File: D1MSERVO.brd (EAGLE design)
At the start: 48.3 x 33 mm, 57 parts, among them IC1 PCA9685

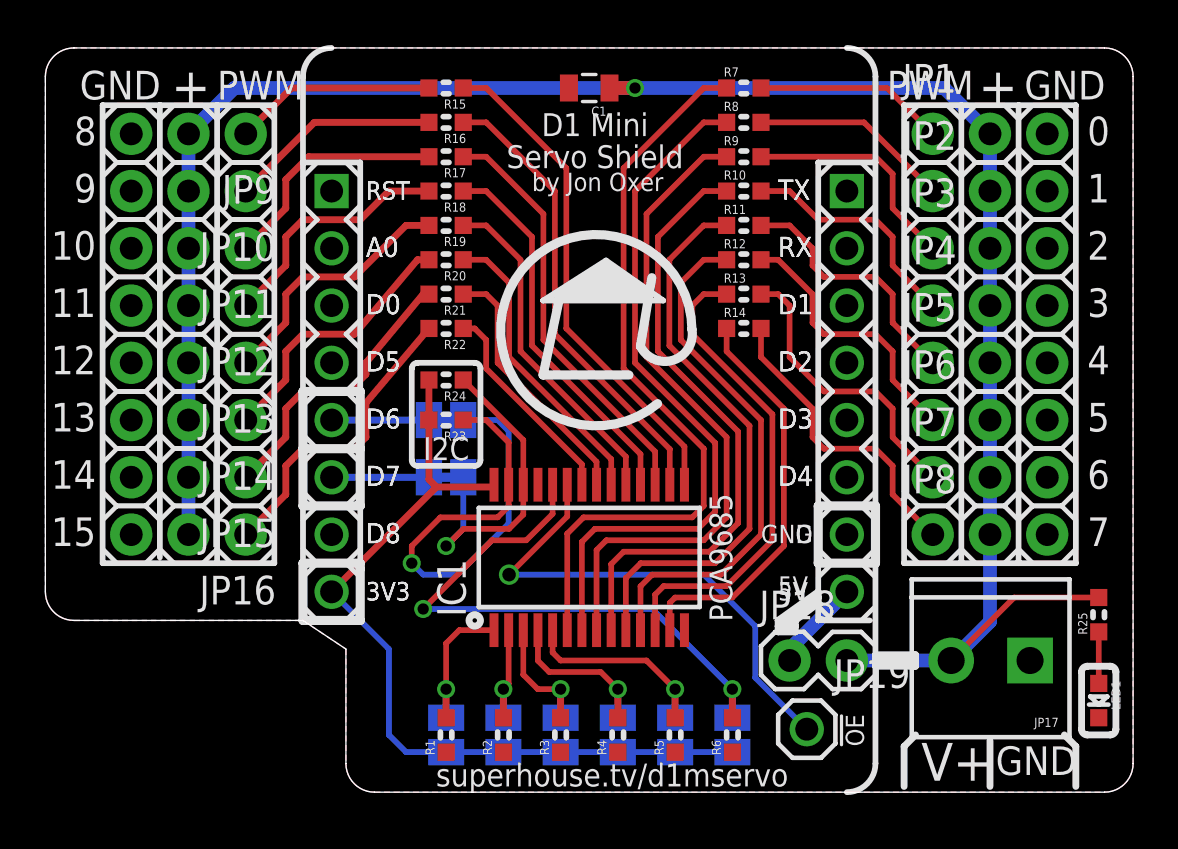
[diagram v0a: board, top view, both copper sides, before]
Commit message: Changed I2C pins
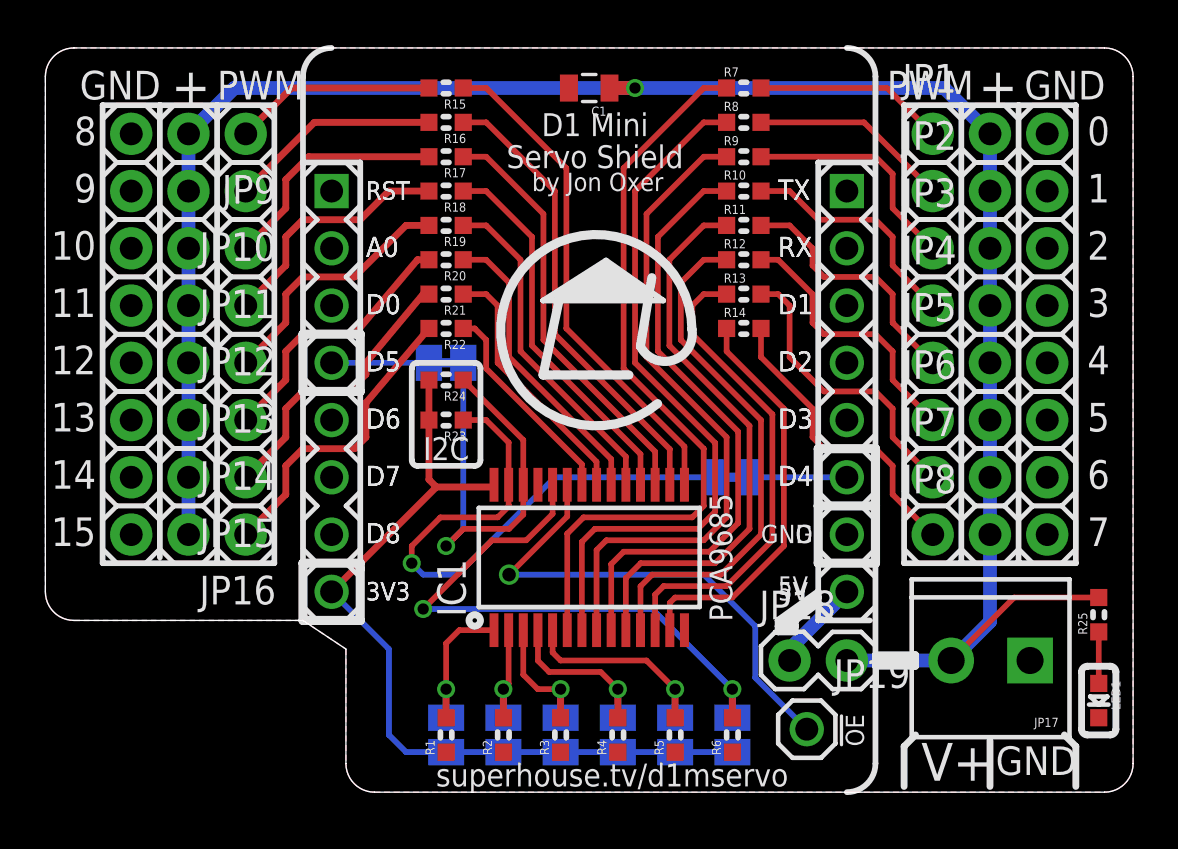
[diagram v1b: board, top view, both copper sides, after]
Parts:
- moved SJ7 13.0 mm to (30.5, 14.0), turned to 0 degrees
- moved SJ8 5.08 mm to (17.8, 19.1)
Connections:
- net D4: now also SJ7.1
- net D5: now also SJ8.1
- net D6: no longer SJ7.1
- net D7: no longer SJ8.1
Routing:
- net SCL: track 14.4 -> 19.5 mm
- net D7: track 4.32 -> 0.00 mm
- net D6: track 4.32 -> 0.00 mm
- net D5: track 0.00 -> 4.32 mm
- net D4: track 0.00 -> 4.32 mm
- net SDA: track 22.9 -> 26.5 mm
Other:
- board text added: "(C)2016 SuperHouse Automation Pty Ltd"
- board text added: "SCL: D5 SDA: D4"
- board text removed: "(C)2016 SuperHouse Pty Ltd"

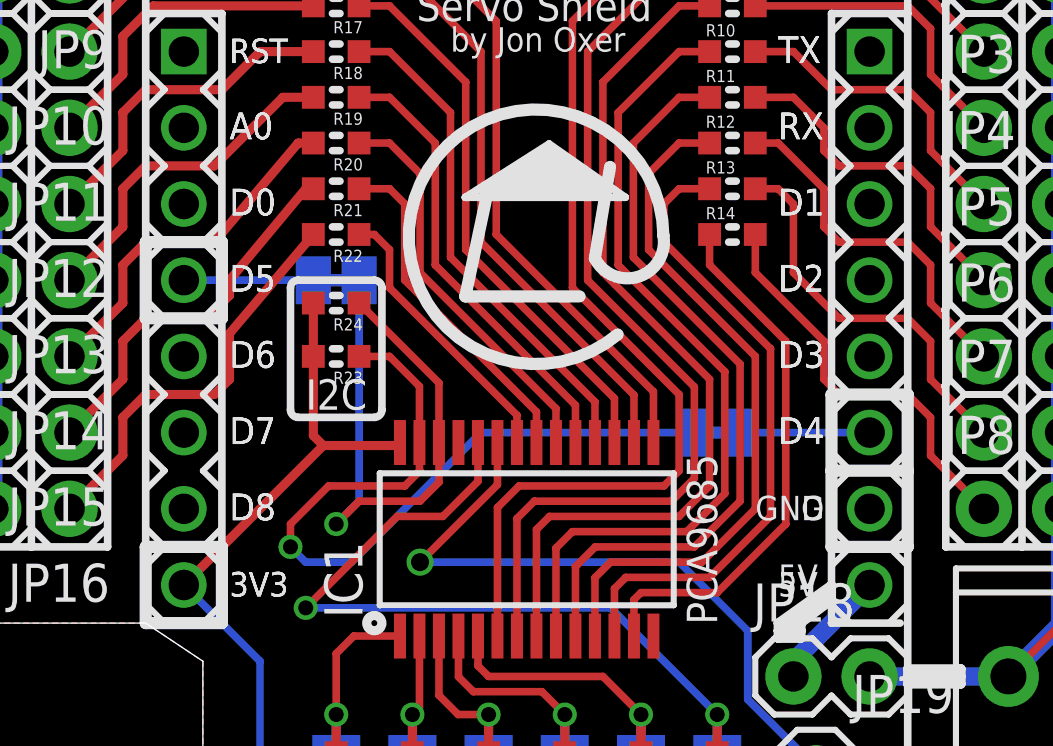
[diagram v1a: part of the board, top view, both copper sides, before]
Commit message: Changed I2C pins (again) to match ESP12E like on the D1 Mini and D1 R2
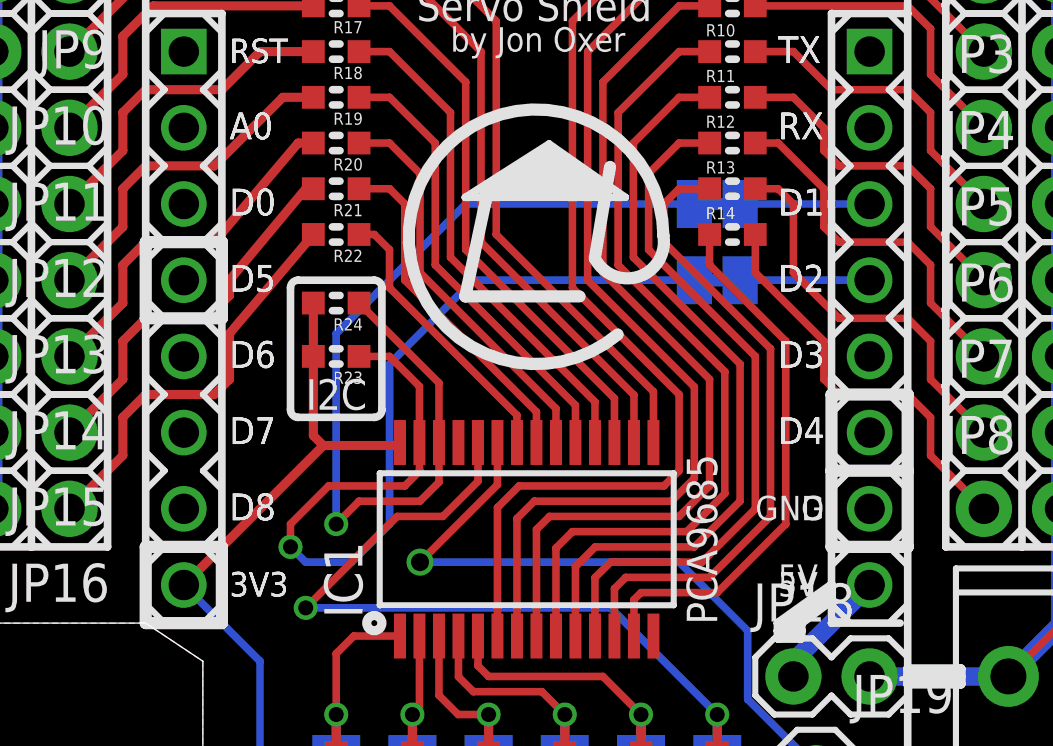
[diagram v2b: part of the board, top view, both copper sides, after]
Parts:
- moved SJ8 13.0 mm to (30.5, 21.6), turned to 0 degrees
- moved SJ7 5.08 mm to (30.5, 19.1)
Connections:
- net D1: now also SJ8.1
- net D2: now also SJ7.1
- net D4: no longer SJ7.1
- net D5: no longer SJ8.1
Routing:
- net SCL: track 19.5 -> 31.2 mm
- net SDA: track 26.5 -> 31.8 mm
- net D5: track 4.32 -> 0.00 mm
- net D4: track 4.32 -> 0.00 mm
- net D2: track 0.00 -> 4.32 mm
- net D1: track 0.00 -> 4.32 mm
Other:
- board text added: "SCL: D1 SDA: D2"
- board text removed: "SCL: D5 SDA: D4"
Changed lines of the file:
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@@
 <grid distance="0.01" unitdist="inch" unit="inch" style="lines" multiple="1" display="yes" altdistance="5" altunitdist="mil" altunit="mil"/>
 <layers>
-<layer number="1" name="Top" color="4" fill="1" visible="no" active="yes"/>
+<layer number="1" name="Top" color="4" fill="1" visible="yes" active="yes"/>
 <layer number="2" name="Route2" color="1" fill="3" visible="no" active="no"/>
 <layer number="3" name="Route3" color="4" fill="3" visible="no" active="no"/>
@@
 <text x="27.94" y="5.08" size="1.016" layer="22" font="vector" ratio="12" rot="MR0" align="bottom-center">A4</text>
 <text x="30.48" y="5.08" size="1.016" layer="22" font="vector" ratio="12" rot="MR0" align="bottom-center">A5</text>
-<text x="22.352" y="18.542" size="1.016" layer="22" font="vector" ratio="12" rot="MR0">SCL</text>
+<text x="28.448" y="21.082" size="1.016" layer="22" font="vector" ratio="12" rot="MR0">SCL</text>
 <text x="14.224" y="26.289" size="0.8128" layer="22" font="vector" ratio="15" rot="MR0" align="bottom-right">RST</text>
 <text x="14.224" y="18.669" size="0.889" layer="22" font="vector" ratio="15" rot="MR0" align="bottom-right">D5</text>
@@
 <wire x1="6.35" y1="9.652" x2="6.35" y2="8.636" width="0.254" layer="22"/>
 <wire x1="6.858" y1="9.144" x2="5.842" y2="9.144" width="0.254" layer="22"/>
-<text x="27.686" y="31.496" size="1.016" layer="22" font="vector" ratio="12" distance="36" rot="MR270">(C)2016 SuperHouse
+<text x="24.892" y="26.416" size="1.016" layer="22" font="vector" ratio="12" distance="36" rot="MR270">(C)2016 SuperHouse
 Automation Pty Ltd</text>
 <text x="24.384" y="27.686" size="1.016" layer="21" font="vector" ratio="18" distance="40" align="bottom-center">D1 Mini
@@
 <text x="21.336" y="31.496" size="0.8128" layer="22" font="vector" ratio="18" rot="MR0">v1.0</text>
 <text x="21.336" y="30.226" size="0.8128" layer="22" font="vector" ratio="18" rot="MR0">SKU: D1MSERVO</text>
-<text x="28.448" y="13.462" size="1.016" layer="22" font="vector" ratio="12" rot="MR0">SDA</text>
+<text x="28.448" y="18.542" size="1.016" layer="22" font="vector" ratio="12" rot="MR0">SDA</text>
 <wire x1="11.43" y1="17.78" x2="11.43" y2="7.62" width="0.254" layer="22"/>
 <wire x1="11.43" y1="17.78" x2="11.43" y2="20.32" width="0.4064" layer="22"/>
@@
 <wire x1="34.29" y1="15.24" x2="36.83" y2="15.24" width="0.4064" layer="22"/>
 <wire x1="36.83" y1="15.24" x2="36.83" y2="12.7" width="0.4064" layer="22"/>
-<text x="21.336" y="27.432" size="1.016" layer="22" font="vector" ratio="12" rot="MR0">SCL: D5
-SDA: D4</text>
+<text x="21.336" y="27.432" size="1.016" layer="22" font="vector" ratio="12" rot="MR0">SCL: D1
+SDA: D2</text>
 <wire x1="11.43" y1="20.32" x2="11.43" y2="17.78" width="0.4064" layer="21"/>
 <wire x1="13.97" y1="17.78" x2="13.97" y2="20.32" width="0.4064" layer="21"/>
@@
 <element name="JP15" library="freetronics-jon" package="1X03" value="" x="8.89" y="13.97" rot="R180"/>
 <element name="JP16" library="freetronics-jon" package="1X03" value="" x="8.89" y="11.43" rot="R180"/>
-<element name="SJ7" library="freetronics-jon" package="SJC" value="SJCN" x="30.48" y="13.97" rot="MR0"/>
-<element name="SJ8" library="freetronics-jon" package="SJC" value="SJCN" x="17.78" y="19.05" rot="MR180"/>
+<element name="SJ7" library="freetronics-jon" package="SJC" value="SJCN" x="30.48" y="19.05" rot="MR0"/>
+<element name="SJ8" library="freetronics-jon" package="SJC" value="SJCN" x="30.48" y="21.59" rot="MR0"/>
 <element name="R23" library="freetronics-jon" package="0603" value="10K" x="17.78" y="16.51" rot="R180"/>
 <element name="R24" library="freetronics-jon" package="0603" value="10K" x="17.78" y="18.288" rot="R180"/>
@@
 <signal name="D1">
 <contactref element="H2" pad="3"/>
+<contactref element="SJ8" pad="1"/>
+<wire x1="31.242" y1="21.59" x2="35.56" y2="21.59" width="0.254" layer="16"/>
 </signal>
 <signal name="D2">
 <contactref element="H2" pad="4"/>
+<contactref element="SJ7" pad="1"/>
+<wire x1="31.242" y1="19.05" x2="35.56" y2="19.05" width="0.254" layer="16"/>
 </signal>
 <signal name="D5">
 <contactref element="H1" pad="4"/>
-<contactref element="SJ8" pad="1"/>
-<wire x1="17.018" y1="19.05" x2="12.7" y2="19.05" width="0.254" layer="16"/>
 </signal>
 <signal name="D6">
@@
 <signal name="D4">
 <contactref element="H2" pad="6"/>
-<contactref element="SJ7" pad="1"/>
-<wire x1="31.242" y1="13.97" x2="35.56" y2="13.97" width="0.254" layer="16"/>
 </signal>
 <signal name="RX">
@@
 <contactref element="SJ7" pad="2"/>
 <contactref element="R23" pad="1"/>
-<wire x1="22.606" y1="13.97" x2="18.288" y2="9.652" width="0.254" layer="16"/>
 <wire x1="18.288" y1="9.652" x2="16.764" y2="9.652" width="0.254" layer="16"/>
 <wire x1="16.764" y1="9.652" x2="16.256" y2="10.16" width="0.254" layer="16"/>
@@
 <wire x1="19.558" y1="16.51" x2="20.555" y2="15.513" width="0.254" layer="1"/>
 <wire x1="20.555" y1="15.513" x2="20.555" y2="13.639" width="0.254" layer="1"/>
-<wire x1="22.606" y1="13.97" x2="29.718" y2="13.97" width="0.254" layer="16"/>
 <wire x1="20.066" y1="12.192" x2="20.555" y2="12.681" width="0.254" layer="1"/>
 <wire x1="20.555" y1="12.681" x2="20.555" y2="13.639" width="0.254" layer="1"/>
+<wire x1="18.288" y1="9.652" x2="19.558" y2="10.922" width="0.254" layer="16"/>
+<wire x1="19.558" y1="10.922" x2="19.558" y2="16.256" width="0.254" layer="16"/>
+<wire x1="19.558" y1="16.256" x2="22.352" y2="19.05" width="0.254" layer="16"/>
+<wire x1="22.352" y1="19.05" x2="29.718" y2="19.05" width="0.254" layer="16"/>
 </signal>
 <signal name="SCL">
@@
 <contactref element="SJ8" pad="2"/>
 <contactref element="R24" pad="1"/>
-<wire x1="18.542" y1="19.05" x2="18.542" y2="11.684" width="0.254" layer="16"/>
-<wire x1="18.542" y1="11.684" x2="17.78" y2="10.922" width="0.254" layer="16"/>
 <via x="17.78" y="10.922" extent="1-16" drill="0.5"/>
 <wire x1="21.205" y1="12.315" x2="21.205" y2="13.639" width="0.254" layer="1"/>
@@
 <wire x1="20.574" y1="11.684" x2="18.542" y2="11.684" width="0.254" layer="1"/>
 <wire x1="18.542" y1="11.684" x2="17.78" y2="10.922" width="0.254" layer="1"/>
+<wire x1="17.78" y1="10.922" x2="17.78" y2="17.272" width="0.254" layer="16"/>
+<wire x1="17.78" y1="17.272" x2="22.098" y2="21.59" width="0.254" layer="16"/>
+<wire x1="22.098" y1="21.59" x2="29.718" y2="21.59" width="0.254" layer="16"/>
 </signal>
 <signal name="N$23">
